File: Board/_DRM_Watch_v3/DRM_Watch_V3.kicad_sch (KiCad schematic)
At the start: 79 parts, among them J1 TYPE-C-31-M-12, J2 687110149022, Q1 2N7002LT1G, U1 ESP32-S2, U3 TP4056, Y1 XRCGB48M000F0Z00R0

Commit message: 2024-01-15 Board: add step-up resistor and cap to RST pin 2024-01-15 Board: quartz bigger package 2024-01-15 Board: add more testpoints for unused pins 2024-01-15 Board: top led: place for smaller led 2024-01-15 Board: move caacitors closer to chips 2024-01-15 Board: make wifi wire thicker 2024-01-15 Board: move wifi antenna closer to chips 2024-01-15 Board: add vias around ANT wire 2024-01-15 Board: move antenna elements closer to chip  2024-01-15 Board: replace onboard antenna by wire soldered on board 2024-01-15 Board: Add jumper to close charger 2024-01-15 Board: Add dm123a chip    (static const uint8_t SDA = 33;   static const uint8_t SCL = 35;)
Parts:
- removed AE1: Antenna, Project-Lib:Texas_SWRA117D_2.4GHz_Right, symbol Device:Antenna_Chip
- added C14: 1uF, Project-Lib:C_0603_1608Metric, symbol Device:C
- added C15: 10uF, Project-Lib:C_0603_1608Metric, symbol Device:C
- added D6: BL1, Project-Lib:SMD-LED-Side-View, symbol Device:LED
- added D7: BL2, Project-Lib:SMD-LED-Side-View, symbol Device:LED
- added JP1: Jumper_2_Open, Project-Lib:SolderJumper-2_P1.3mm_Open_Pad1.0x1.5mm, symbol Jumper:Jumper_2_Open
- added R16: 10K, Project-Lib:R_0603_1608Metric, symbol Device:R
- added R17, R18: R22, Project-Lib:R_0603_1608Metric, symbol Device:R
- added TP27: ANT, Project-Lib:TestPoint_Pad, symbol Project-Lib:TestPoint
- added TP28: ANT2, Project-Lib:TestPoint_Pad, symbol Project-Lib:TestPoint
- added TP29: SDA, Project-Lib:TestPoint_Pad, symbol Project-Lib:TestPoint
- added TP30: SCL, Project-Lib:TestPoint_Pad, symbol Project-Lib:TestPoint
- added TP31: D14, Project-Lib:TestPoint_Pad, symbol Project-Lib:TestPoint
- added TP32: D17, Project-Lib:TestPoint_Pad, symbol Project-Lib:TestPoint
- added TP33: D18, Project-Lib:TestPoint_Pad, symbol Project-Lib:TestPoint
- added TP34: D21, Project-Lib:TestPoint_Pad, symbol Project-Lib:TestPoint
- added TP35: D45, Project-Lib:TestPoint_Pad, symbol Project-Lib:TestPoint
- added TP36: D34, Project-Lib:TestPoint_Pad, symbol Project-Lib:TestPoint
- added TP37: D13, Project-Lib:TestPoint_Pad, symbol Project-Lib:TestPoint
- added TP38: BL2, Project-Lib:TestPoint_Pad, symbol Project-Lib:TestPoint
- added U4: DS3231S, Project-Lib:SOIC127P1032X265-16N, symbol Project-Lib:DS3231S
- D1: footprint Project-Lib:SMD-LED-Side-View -> Project-Lib:HOLE_LED_0805_2012Metric
- TP10: value RST -> EN
- TP11: value SENS-BAT -> S.BAT
- TP12: value SENS-USB -> S.USB
- TP26: value TP_CE -> BL1
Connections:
- net +3V3: now also C15.2, R16.1, U4.2 (VCC)
- net GND: now also C14.1, C15.1, D6.1 (K), D7.1 (K), U4.10 (N.C.), U4.11 (N.C.), U4.12 (N.C.), U4.13 (GND), U4.5 (N.C.), U4.6 (N.C.), U4.7 (N.C.), U4.8 (N.C.), U4.9 (N.C.)
- net VBUS: now also R7.1, R8.1, U3.8 (CE), JP1.1 (A); no longer D3.2 (A), D4.2 (A)
- net VCC: now also JP1.2 (B)
- net at R10.2, TP21.1: now also U1.42 (GPIO38); no longer U1.39 (GPIO35)
- net at S3.2, TP10.1, U1.56 (CHIP_PU/RESET): now also C14.2, R16.2
- net at U1.18 (GPIO13/ADC2_CH2): now also TP37.1
- net at U1.19 (GPIO14/ADC2_CH3): now also TP31.1
- net at U1.23 (GPIO17/ADC2_CH6/DAC_1): now also TP32.1
- net at U1.24 (GPIO18/ADC2_CH7/DAC_2): now also TP33.1
- net at U1.28 (GPIO21): now also TP34.1
- net at U1.35 (SPIQ/GPIO31): now also TP26.1, R17.2
- net at U1.36 (SPID/GPIO32): now also R18.2, TP38.1
- net at R5.2, TP19.1: now also U1.40 (GPIO36); no longer U1.37 (GPIO33)
- net at R6.2, TP20.1: now also U1.41 (GPIO37); no longer U1.38 (GPIO34)
- net at U1.50 (GPIO45): now also TP35.1
- net at U3.6 (STDBY): now also D3.2 (A); no longer R7.1
- net at U3.7 (CHRGE): now also D4.2 (A); no longer R8.1
- net at C13.2, R15.1: now also TP27.1
- new net: TP30.1, U1.39 (GPIO35), U4.16 (SCL)
- new net: TP29.1, U1.37 (GPIO33), U4.15 (SDA)
- new net: TP36.1, U1.38 (GPIO34)
- new net: D6.2 (A), R17.1
- new net: D7.2 (A), R18.1
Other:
- note added: "ANTENNA ZONE"
- note added: "BACKLIGHT ZONE"
- note added: "RTC ZONE"
- note added: "TP ZONE"
- moved on the sheet: C11, C12, D1, D2, D3, D4, D5, LS1, M1, M2, M3, Q1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

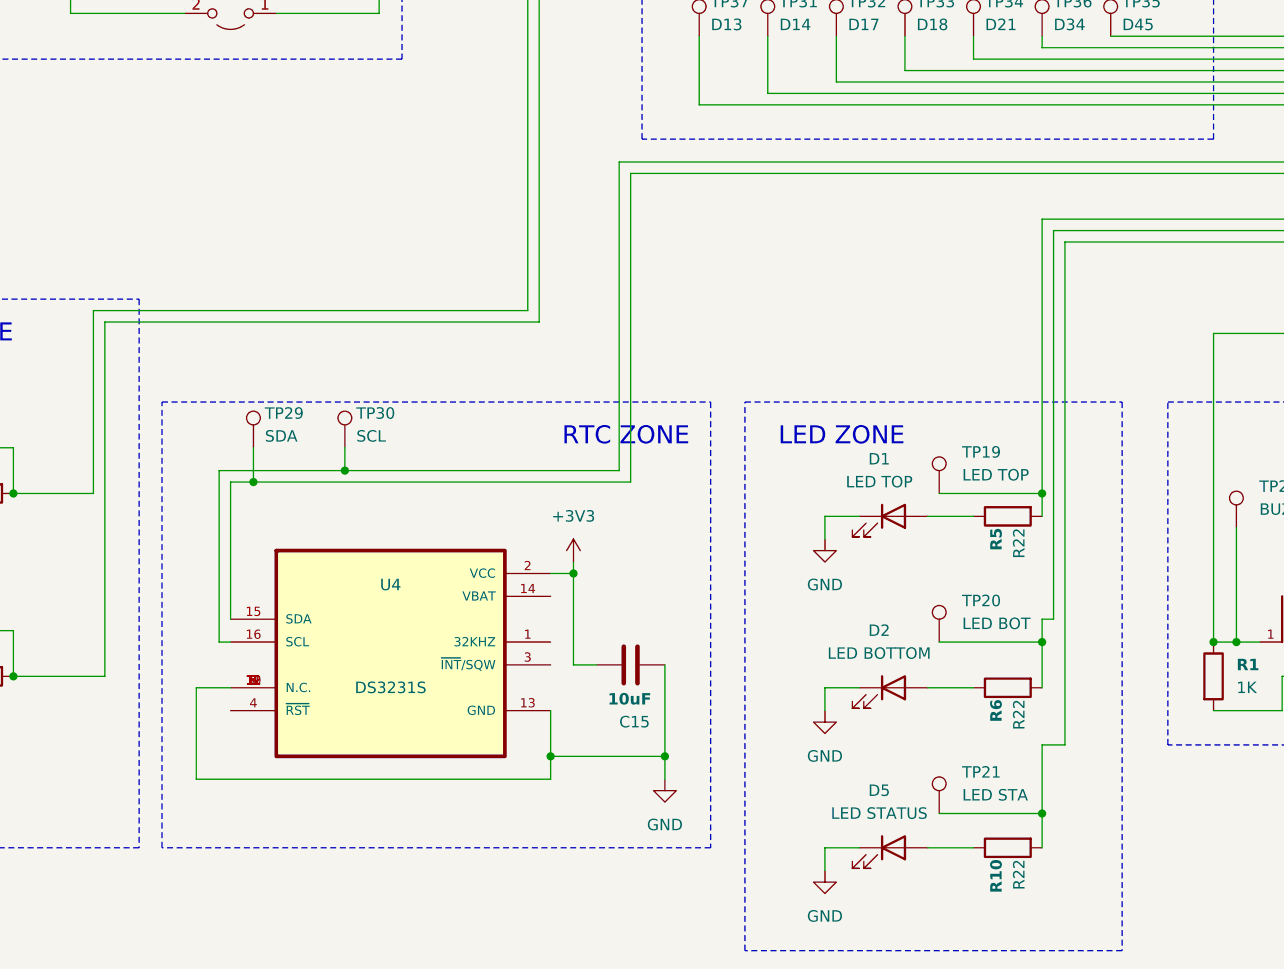
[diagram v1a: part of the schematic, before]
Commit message: 2024-02-03 v0.23 Stopwatch fixed 2024-02-03 v0.23 updated init led effect 2024-02-03 v0.23 added value showing time since last charging 2024-02-03 v0.23 replaced back icon 2024-02-03 v0.23 started implementing of alert functionality
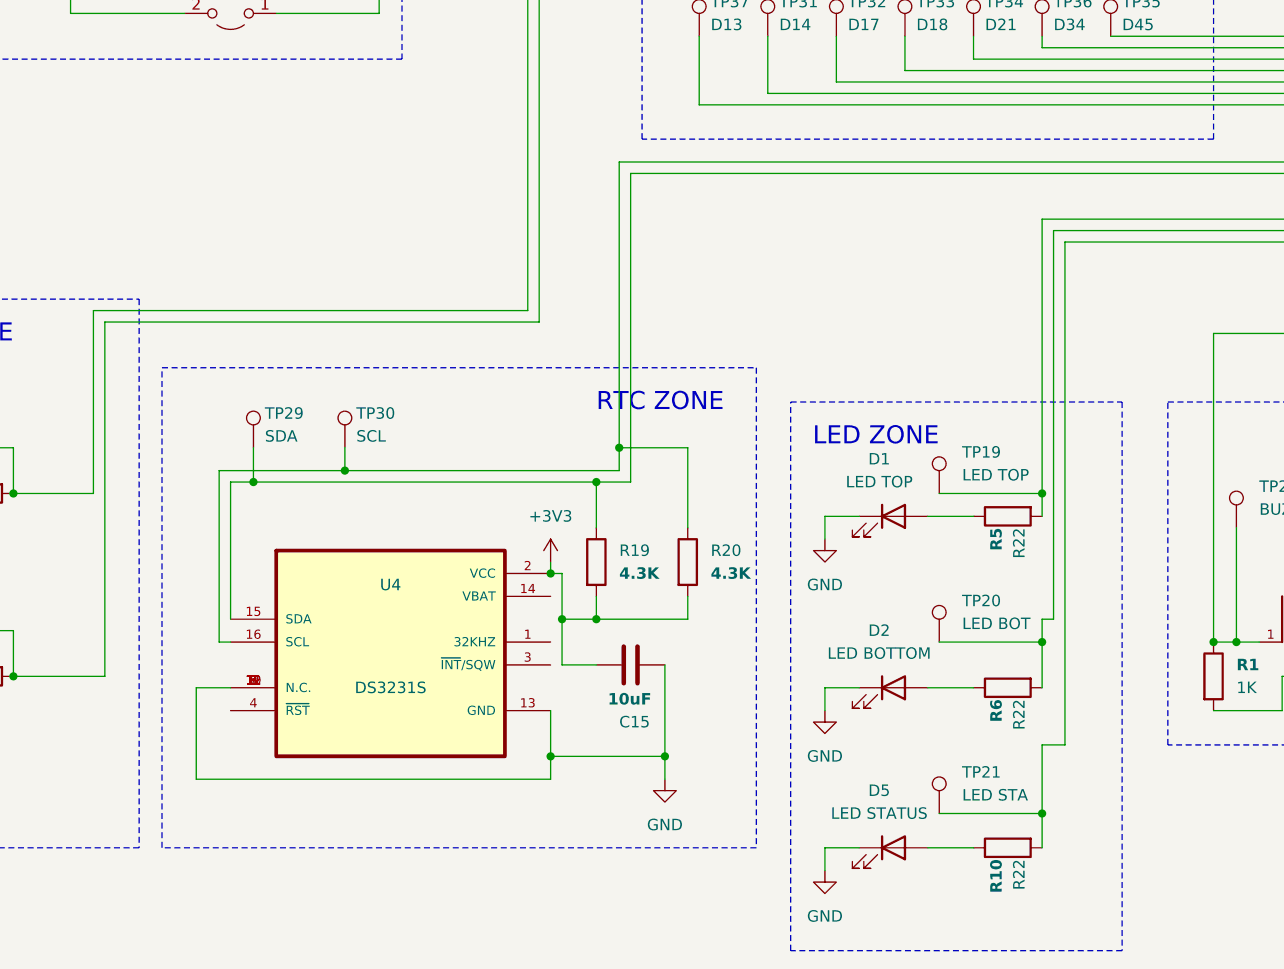
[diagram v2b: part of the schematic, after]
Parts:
- added R19, R20: 4.3K, Project-Lib:R_0603_1608Metric, symbol Device:R
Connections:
- net +3V3: now also R19.2, R20.2
- net at TP30.1, U1.39 (GPIO35), U4.16 (SCL): now also R20.1
- net at TP29.1, U1.37 (GPIO33), U4.15 (SDA): now also R19.1
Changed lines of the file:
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@@
   (junction (at 346.71 125.73) (diameter 0) (color 0 0 0 0)
   )
+  (junction (at 140.97 223.52) (diameter 0) (color 0 0 0 0)
+  )
   (junction (at 339.09 200.66) (diameter 0) (color 0 0 0 0)
   )
@@
   (junction (at 337.82 34.29) (diameter 0) (color 0 0 0 0)
   )
-  (junction (at 138.43 233.68) (diameter 0) (color 0 0 0 0)
-  )
   (junction (at 171.45 20.32) (diameter 0) (color 0 0 0 0)
   )
@@
   (junction (at 190.5 241.3) (diameter 0) (color 0 0 0 0)
   )
+  (junction (at 140.97 238.76) (diameter 0) (color 0 0 0 0)
+  )
   (junction (at 73.66 86.36) (diameter 0) (color 0 0 0 0)
   )
@@
   (junction (at 73.66 97.79) (diameter 0) (color 0 0 0 0)
   )
+  (junction (at 135.89 233.68) (diameter 0) (color 0 0 0 0)
+  )
   (junction (at 59.69 152.4) (diameter 0) (color 0 0 0 0)
   )
@@
   (junction (at 50.8 245.11) (diameter 0) (color 0 0 0 0)
   )
+  (junction (at 137.16 238.76) (diameter 0) (color 0 0 0 0)
+  )
   (junction (at 220.98 245.11) (diameter 0) (color 0 0 0 0)
   )
@@
   (junction (at 30.48 90.17) (diameter 0) (color 0 0 0 0)
   )
+  (junction (at 143.51 219.71) (diameter 0) (color 0 0 0 0)
+  )
   (wire (pts (xy 88.9 134.62) (xy 88.9 152.4))
     (stroke (width 0) (type default))
@@
     (stroke (width 0) (type default))
   )
+  (wire (pts (xy 140.97 236.22) (xy 140.97 238.76))
+    (stroke (width 0) (type default))
+  )
   (wire (pts (xy 191.77 238.76) (xy 190.5 238.76))
     (stroke (width 0) (type default))
@@
     (stroke (width 0) (type default))
   )
+  (wire (pts (xy 143.51 219.71) (xy 143.51 222.25))
+    (stroke (width 0) (type default))
+  )
   (wire (pts (xy 342.9 90.17) (xy 342.9 110.49))
     (stroke (width 0) (type default))
@@
     (stroke (width 0) (type default))
   )
-  (wire (pts (xy 138.43 243.84) (xy 140.97 243.84))
+  (wire (pts (xy 137.16 243.84) (xy 140.97 243.84))
     (stroke (width 0) (type default))
   )
@@
     (stroke (width 0) (type default))
   )
-  (wire (pts (xy 138.43 233.68) (xy 138.43 232.41))
+  (wire (pts (xy 135.89 233.68) (xy 135.89 232.41))
     (stroke (width 0) (type default))
   )
@@
     (stroke (width 0) (type default))
   )
+  (wire (pts (xy 151.13 238.76) (xy 140.97 238.76))
+    (stroke (width 0) (type default))
+  )
   (wire (pts (xy 83.82 149.86) (xy 86.36 149.86))
     (stroke (width 0) (type default))
@@
     (stroke (width 0) (type default))
   )
-  (wire (pts (xy 135.89 233.68) (xy 138.43 233.68))
+  (wire (pts (xy 135.89 233.68) (xy 137.16 233.68))
     (stroke (width 0) (type default))
   )
@@
     (stroke (width 0) (type default))
   )
-  (wire (pts (xy 138.43 233.68) (xy 138.43 243.84))
+  (wire (pts (xy 137.16 233.68) (xy 137.16 238.76))
     (stroke (width 0) (type default))
   )
@@
     (stroke (width 0) (type default))
   )
+  (wire (pts (xy 151.13 219.71) (xy 143.51 219.71))
+    (stroke (width 0) (type default))
+  )
   (wire (pts (xy 134.62 148.59) (xy 134.62 205.74))
     (stroke (width 0) (type default))
@@
     (stroke (width 0) (type default))
   )
+  (wire (pts (xy 151.13 236.22) (xy 151.13 238.76))
+    (stroke (width 0) (type default))
+  )
   (wire (pts (xy 283.21 195.58) (xy 334.01 195.58))
     (stroke (width 0) (type default))
@@
     (stroke (width 0) (type default))
   )
-  (wire (pts (xy 143.51 187.96) (xy 143.51 222.25))
+  (wire (pts (xy 143.51 187.96) (xy 143.51 219.71))
     (stroke (width 0) (type default))
   )
@@
     (stroke (width 0) (type default))
   )
+  (wire (pts (xy 140.97 223.52) (xy 140.97 228.6))
+    (stroke (width 0) (type default))
+  )
   (wire (pts (xy 63.5 224.79) (xy 68.58 224.79))
     (stroke (width 0) (type default))
@@
     (stroke (width 0) (type default))
   )
+  (wire (pts (xy 140.97 223.52) (xy 102.87 223.52))
+    (stroke (width 0) (type default))
+  )
   (wire (pts (xy 214.63 241.3) (xy 212.09 241.3))
     (stroke (width 0) (type default))
@@
     (stroke (width 0) (type default))
   )
-  (wire (pts (xy 144.78 223.52) (xy 102.87 223.52))
+  (wire (pts (xy 144.78 223.52) (xy 140.97 223.52))
     (stroke (width 0) (type default))
   )
@@
     (stroke (width 0) (type default))
   )
+  (wire (pts (xy 137.16 238.76) (xy 137.16 243.84))
+    (stroke (width 0) (type default))
+  )
   (wire (pts (xy 363.22 208.28) (xy 347.98 208.28))
     (stroke (width 0) (type default))
@@
     (stroke (width 0) (type default))
   )
+  (wire (pts (xy 151.13 228.6) (xy 151.13 219.71))
+    (stroke (width 0) (type default))
+  )
   (wire (pts (xy 87.63 102.87) (xy 87.63 99.06))
     (stroke (width 0) (type default))
@@
     (stroke (width 0) (type default))
   )
+  (wire (pts (xy 140.97 238.76) (xy 137.16 238.76))
+    (stroke (width 0) (type default))
+  )
   (wire (pts (xy 171.45 53.34) (xy 168.91 53.34))
     (stroke (width 0) (type default))
@@
     (fill (type none))
   )
-  (rectangle (start 157.48 214.63) (end 199.39 275.59)
+  (rectangle (start 162.56 214.63) (end 199.39 275.59)
     (stroke (width 0) (type dash) (color 132 132 132 1))
     (fill (type none))
@@
     (fill (type none))
   )
-  (rectangle (start 92.71 214.63) (end 153.67 264.16)
+  (rectangle (start 92.71 210.82) (end 158.75 264.16)
     (stroke (width 0) (type dash) (color 132 132 132 1))
     (fill (type none))
@@
     (effects (font (size 2 2)) (justify left bottom))
   )
-  (text "LED ZONE" (at 175.26 219.71 0)
+  (text "LED ZONE" (at 179.07 219.71 0)
     (effects (font (size 2 2)) (justify right bottom))
   )
@@
     (effects (font (size 2 2)) (justify left bottom))
   )
-  (text "RTC ZONE" (at 137.16 219.71 0)
+  (text "RTC ZONE" (at 140.97 215.9 0)
     (effects (font (size 2 2)) (justify left bottom))
   )
@@
     )
   )
+  (symbol (lib_id "Device:R") (at 151.13 232.41 0) (unit 1)
+    (in_bom yes) (on_board yes) (dnp no)
+    (property "Reference" "R20" (at 153.67 231.14 0)
+      (effects (font (size 1.27 1.27)) (justify left))
+    )
+    (property "Value" "4.3K" (at 153.67 233.68 0)
+      (effects (font (size 1.27 1.27) bold) (justify left))
+    )
+    (property "Footprint" "Project-Lib:R_0603_1608Metric" (at 149.352 232.41 90)
+      (effects (font (size 1.27 1.27)) hide)
+    )
+    (property "Datasheet" "~" (at 151.13 232.41 0)
+      (effects (font (size 1.27 1.27)) hide)
+    )
+    (property "Role" "Pull-Up for RTC SCL" (at 151.13 232.41 0)
+      (effects (font (size 1.27 1.27)) hide)
+    )
+    (pin "1")
+    (pin "2")
+    (instances
+      (project "DRM_Watch_V3"
+        (path "/d50c768c-843d-4a19-b0bf-8bd21b6b9231"
+          (reference "R20") (unit 1)
+        )
+      )
+    )
+  )
   (symbol (lib_id "power:GND") (at 379.73 175.26 0) (unit 1)
     (in_bom yes) (on_board yes) (dnp no)
@@
     )
   )
-  (symbol (lib_id "power:+3V3") (at 138.43 232.41 0) (unit 1)
+  (symbol (lib_id "power:+3V3") (at 135.89 232.41 0) (unit 1)
     (in_bom yes) (on_board yes) (dnp no) (fields_autoplaced)
-    (property "Reference" "#PWR040" (at 138.43 236.22 0)
+    (property "Reference" "#PWR040" (at 135.89 236.22 0)
       (effects (font (size 1.27 1.27)) hide)
     )
-    (property "Value" "+3V3" (at 138.43 227.33 0)
+    (property "Value" "+3V3" (at 135.89 227.33 0)
       (effects (font (size 1.27 1.27)))
     )
-    (property "Footprint" "" (at 138.43 232.41 0)
+    (property "Footprint" "" (at 135.89 232.41 0)
       (effects (font (size 1.27 1.27)) hide)
     )
-    (property "Datasheet" "" (at 138.43 232.41 0)
+    (property "Datasheet" "" (at 135.89 232.41 0)
       (effects (font (size 1.27 1.27)) hide)
     )
@@
         )
       )
+    )
+  )
+  (symbol (lib_id "Device:R") (at 140.97 232.41 0) (unit 1)
+    (in_bom yes) (on_board yes) (dnp no)
+    (property "Reference" "R19" (at 143.51 231.14 0)
+      (effects (font (size 1.27 1.27)) (justify left))
+    )
+    (property "Value" "4.3K" (at 143.51 233.68 0)
+      (effects (font (size 1.27 1.27) bold) (justify left))
+    )
+    (property "Footprint" "Project-Lib:R_0603_1608Metric" (at 139.192 232.41 90)
+      (effects (font (size 1.27 1.27)) hide)
+    )
+    (property "Datasheet" "~" (at 140.97 232.41 0)
+      (effects (font (size 1.27 1.27)) hide)
+    )
+    (property "Role" "Pull-Up for RTC SDA" (at 140.97 232.41 0)
+      (effects (font (size 1.27 1.27)) hide)
+    )
+    (pin "1")
+    (pin "2")
+    (instances
+      (project "DRM_Watch_V3"
+        (path "/d50c768c-843d-4a19-b0bf-8bd21b6b9231"
+          (reference "R19") (unit 1)
+        )
+      )

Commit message: bosrd
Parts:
- removed D6: BL1, Project-Lib:SMD-LED-Side-View, symbol Device:LED
- removed D7: BL2, Project-Lib:SMD-LED-Side-View, symbol Device:LED
- removed R17, R18: R22, Project-Lib:R_0603_1608Metric, symbol Device:R
- removed T1, T2, T3: ~, Project-Lib:Touch-Region, symbol Project-Lib:touch-region
- removed TP26: BL1, Project-Lib:TestPoint_Pad, symbol Project-Lib:TestPoint
- removed TP32: D17, Project-Lib:TestPoint_Pad, symbol Project-Lib:TestPoint
- removed TP38: BL2, Project-Lib:TestPoint_Pad, symbol Project-Lib:TestPoint
- added C16: 12nF 200V, Capacitor_SMD:C_1206_3216Metric, symbol Device:C_Small
- added U5: ~, Package_DFN_QFN:QFN-16-1EP_4x4mm_P0.65mm_EP2.5x2.5mm, symbol Project-Lib:HV816K6
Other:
- note removed: "TOUCH ZONE"
- moved on the sheet: C15, D1, D2, D5, LS1, Q1, R1, R10, R19, R20, R4, R5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
